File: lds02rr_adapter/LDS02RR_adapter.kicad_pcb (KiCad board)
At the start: 2 copper layers, 18.9 x 8.8 mm, 4 parts, among them J2 JST PH F 4P VERT, Q1 AS2302

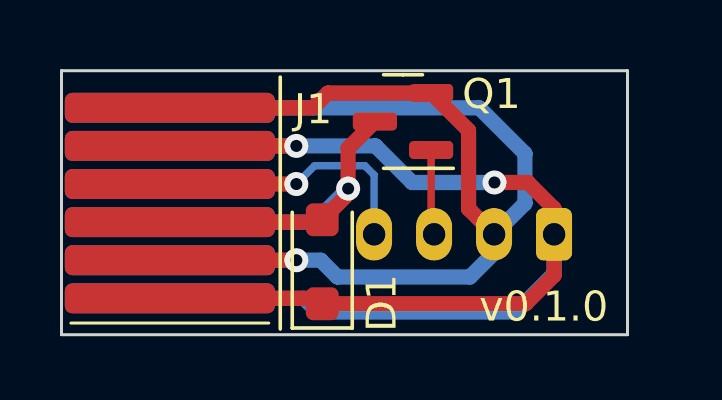
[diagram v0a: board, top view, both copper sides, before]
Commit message: Neato, LDS02RR v0.2.0
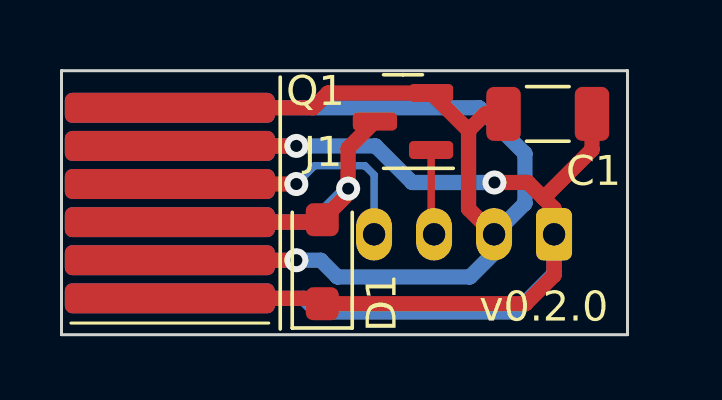
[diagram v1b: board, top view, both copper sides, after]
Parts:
- added C1: 100uF, Capacitor_SMD:C_1206_3216Metric, F.Cu at (156.2, 91.4)
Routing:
- net +5V: track 48.2 -> 51.7 mm
- net GND: track 46.3 -> 47.7 mm
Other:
- board text added: "v0.2.0"
- board text removed: "v0.1.0"
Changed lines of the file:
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@@
     (thickness 1.6)
   )
-  (paper "A4")
+  (paper "A5")
   (title_block
     (title "LDS02RR adapter")
-    (date "2023-12-21")
-    (rev "0.1.0")
+    (date "2024-01-30")
+    (rev "0.2.0")
     (company "Maker's Pet")
     (comment 1 "makerspet.com")
@@
       (drillshape 0)
       (scaleselection 1)
-      (outputdirectory "")
+      (outputdirectory "output/")
     )
   )
@@
     (property "ki_keywords" "LDS")
     (attr smd)
-    (fp_text reference "J1" (at 3.1242 4.7752 180) (layer "F.SilkS")
+    (fp_text reference "J1" (at 1.7018 5.1054 180) (layer "F.SilkS")
         (effects (font (size 1 1) (thickness 0.15)))
     )
@@
       (net 3 "GND") (pinfunction "GND") (pintype "passive") (thermal_bridge_angle 45))
   )
+  (footprint "Capacitor_SMD:C_1206_3216Metric" (layer "F.Cu")
+    (at 156.21 91.44 180)
+    (descr "Capacitor SMD 1206 (3216 Metric), square (rectangular) end terminal, IPC_7351 nominal, (Body size source: IPC-SM-782 page 76, https://www.pcb-3d.com/wordpress/wp-content/uploads/ipc-sm-782a_amendment_1_and_2.pdf), generated with kicad-footprint-generator")
+    (tags "capacitor")
+    (property "Sheetfile" "LDS02RR_adapter.kicad_sch")
+    (property "Sheetname" "")
+    (property "ki_description" "Unpolarized capacitor")
+    (property "ki_keywords" "cap capacitor")
+    (attr smd)
+    (fp_text reference "C1" (at -1.524 -1.905) (layer "F.SilkS")
+        (effects (font (size 1 1) (thickness 0.15)))
+    )
+    (fp_text value "100uF" (at 0 1.85) (layer "F.Fab") hide
+        (effects (font (size 1 1) (thickness 0.15)))
+    )
+    (fp_text user "${REFERENCE}" (at 0 0) (layer "F.Fab")
+        (effects (font (size 0.8 0.8) (thickness 0.12)))
+    )
+    (fp_line (start -0.711252 -0.91) (end 0.711252 -0.91)
+      (stroke (width 0.12) (type solid)) (layer "F.SilkS"))
+    (fp_line (start -0.711252 0.91) (end 0.711252 0.91)
+      (stroke (width 0.12) (type solid)) (layer "F.SilkS"))
+    (fp_line (start -2.3 -1.15) (end 2.3 -1.15)
+      (stroke (width 0.05) (type solid)) (layer "F.CrtYd"))
+    (fp_line (start -2.3 1.15) (end -2.3 -1.15)
+      (stroke (width 0.05) (type solid)) (layer "F.CrtYd"))
+    (fp_line (start 2.3 -1.15) (end 2.3 1.15)
+      (stroke (width 0.05) (type solid)) (layer "F.CrtYd"))
+    (fp_line (start 2.3 1.15) (end -2.3 1.15)
+      (stroke (width 0.05) (type solid)) (layer "F.CrtYd"))
+    (fp_line (start -1.6 -0.8) (end 1.6 -0.8)
+      (stroke (width 0.1) (type solid)) (layer "F.Fab"))
+    (fp_line (start -1.6 0.8) (end -1.6 -0.8)
+      (stroke (width 0.1) (type solid)) (layer "F.Fab"))
+    (fp_line (start 1.6 -0.8) (end 1.6 0.8)
+      (stroke (width 0.1) (type solid)) (layer "F.Fab"))
+    (fp_line (start 1.6 0.8) (end -1.6 0.8)
+      (stroke (width 0.1) (type solid)) (layer "F.Fab"))
+    (pad "1" smd roundrect (at -1.475 0 180) (size 1.15 1.8) (layers "F.Cu" "F.Paste" "F.Mask") (roundrect_rratio 0.2173913043)
+      (net 1 "+5V") (pintype "passive"))
+    (pad "2" smd roundrect (at 1.475 0 180) (size 1.15 1.8) (layers "F.Cu" "F.Paste" "F.Mask") (roundrect_rratio 0.2173913043)
+      (net 3 "GND") (pintype "passive"))
+    (model "${KICAD6_3DMODEL_DIR}/Capacitor_SMD.3dshapes/C_1206_3216Metric.wrl"
+      (offset (xyz 0 0 0))
+      (scale (xyz 1 1 1))
+      (rotate (xyz 0 0 0))
+    )
+  )
   (footprint "Diode_SMD:D_SOD-123F" (layer "F.Cu")
     (at 148.6916 96.3676 90)
@@
     (property "ki_keywords" "N-Channel MOSFET")
     (attr smd)
-    (fp_text reference "Q1" (at -2.9464 0.9144) (layer "F.SilkS")
+    (fp_text reference "Q1" (at 2.921 1.016) (layer "F.SilkS")
         (effects (font (size 1 1) (thickness 0.15)))
     )
@@
     (effects (font (size 1 1) (thickness 0.15)) (justify left bottom mirror))
   )
-  (gr_text "v0.1.0" (at 153.924 98.4504) (layer "F.SilkS")
+  (gr_text "v0.2.0" (at 153.924 98.4504) (layer "F.SilkS")
     (effects (font (size 1 1) (thickness 0.15)) (justify left bottom))
   )
+  (segment (start 157.685 92.632) (end 156.0703 94.2467) (width 0.508) (layer "F.Cu") (net 1))
   (segment (start 155.4704 97.7676) (end 156.4188 96.8192) (width 0.508) (layer "F.Cu") (net 1))
   (segment (start 143.6116 97.5868) (end 148.5108 97.5868) (width 0.508) (layer "F.Cu") (net 1))
   (segment (start 155.5496 93.726) (end 154.432 93.726) (width 0.508) (layer "F.Cu") (net 1))
+  (segment (start 156.0703 94.2467) (end 156.4188 94.5952) (width 0.508) (layer "F.Cu") (net 1))
   (segment (start 156.4188 94.5952) (end 156.4188 95.4532) (width 0.508) (layer "F.Cu") (net 1))
   (segment (start 148.7424 97.7676) (end 155.4704 97.7676) (width 0.508) (layer "F.Cu") (net 1))
-  (segment (start 155.5496 93.726) (end 156.4188 94.5952) (width 0.508) (layer "F.Cu") (net 1))
+  (segment (start 157.685 91.44) (end 157.685 92.632) (width 0.508) (layer "F.Cu") (net 1))
   (segment (start 148.5108 97.5868) (end 148.6916 97.7676) (width 0.508) (layer "F.Cu") (net 1))
+  (segment (start 155.5496 93.726) (end 156.0703 94.2467) (width 0.508) (layer "F.Cu") (net 1))
   (segment (start 156.4188 96.8192) (end 156.4188 95.4532) (width 0.508) (layer "F.Cu") (net 1))
   (segment (start 143.6116 92.5068) (end 147.828 92.5068) (width 0.508) (layer "F.Cu") (net 1))
@@
   (segment (start 143.6116 95.0468) (end 148.4376 95.0468) (width 0.508) (layer "B.Cu") (net 2))
   (segment (start 148.4376 95.0468) (end 149.5552 93.9292) (width 0.508) (layer "B.Cu") (net 2))
+  (segment (start 154.735 91.44) (end 154.1193 91.44) (width 0.508) (layer "F.Cu") (net 3))
   (segment (start 153.5684 91.9909) (end 153.5684 94.6028) (width 0.508) (layer "F.Cu") (net 3))
   (segment (start 153.5684 94.6028) (end 154.4188 95.4532) (width 0.508) (layer "F.Cu") (net 3))
   (segment (start 152.3215 90.744) (end 153.5684 91.9909) (width 0.508) (layer "F.Cu") (net 3))
   (segment (start 143.6116 91.2368) (end 148.3868 91.2368) (width 0.508) (layer "F.Cu") (net 3))
+  (segment (start 154.1193 91.44) (end 153.5684 91.9909) (width 0.508) (layer "F.Cu") (net 3))
   (segment (start 148.8796 90.744) (end 152.3215 90.744) (width 0.508) (layer "F.Cu") (net 3))
   (segment (start 143.6116 96.3168) (end 147.828 96.3168) (width 0.508) (layer "F.Cu") (net 3))

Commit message: 0603 bypass cap
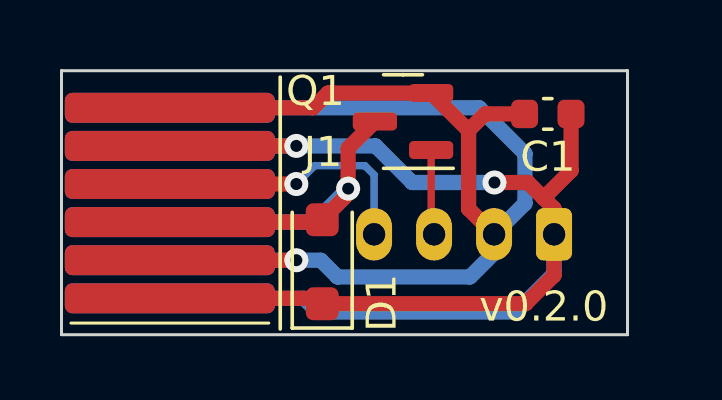
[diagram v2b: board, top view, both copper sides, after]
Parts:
- C1: value 100uF -> 22uF; footprint Capacitor_SMD:C_1206_3216Metric -> Capacitor_SMD:C_0603_1608Metric
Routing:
- net GND: track 47.7 -> 48.4 mm
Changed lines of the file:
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@@
   (title_block
     (title "LDS02RR adapter")
-    (date "2024-01-30")
-    (rev "0.2.0")
+    (date "2024-03-06")
+    (rev "0.2.1")
     (company "Maker's Pet")
     (comment 1 "makerspet.com")
@@
       (net 3 "GND") (pinfunction "GND") (pintype "passive") (thermal_bridge_angle 45))
   )
-  (footprint "Capacitor_SMD:C_1206_3216Metric" (layer "F.Cu")
+  (footprint "Capacitor_SMD:C_0603_1608Metric" (layer "F.Cu")
     (at 156.21 91.44 180)
-    (descr "Capacitor SMD 1206 (3216 Metric), square (rectangular) end terminal, IPC_7351 nominal, (Body size source: IPC-SM-782 page 76, https://www.pcb-3d.com/wordpress/wp-content/uploads/ipc-sm-782a_amendment_1_and_2.pdf), generated with kicad-footprint-generator")
+    (descr "Capacitor SMD 0603 (1608 Metric), square (rectangular) end terminal, IPC_7351 nominal, (Body size source: IPC-SM-782 page 76, https://www.pcb-3d.com/wordpress/wp-content/uploads/ipc-sm-782a_amendment_1_and_2.pdf), generated with kicad-footprint-generator")
     (tags "capacitor")
     (property "Sheetfile" "LDS02RR_adapter.kicad_sch")
@@
     (property "ki_keywords" "cap capacitor")
     (attr smd)
-    (fp_text reference "C1" (at -1.524 -1.905) (layer "F.SilkS")
-        (effects (font (size 1 1) (thickness 0.15)))
-    )
-    (fp_text value "100uF" (at 0 1.85) (layer "F.Fab") hide
-        (effects (font (size 1 1) (thickness 0.15)))
-    )
-    (fp_text user "${REFERENCE}" (at 0 0) (layer "F.Fab")
-        (effects (font (size 0.8 0.8) (thickness 0.12)))
-    )
-    (fp_line (start -0.711252 -0.91) (end 0.711252 -0.91)
-      (stroke (width 0.12) (type solid)) (layer "F.SilkS"))
-    (fp_line (start -0.711252 0.91) (end 0.711252 0.91)
-      (stroke (width 0.12) (type solid)) (layer "F.SilkS"))
-    (fp_line (start -2.3 -1.15) (end 2.3 -1.15)
-      (stroke (width 0.05) (type solid)) (layer "F.CrtYd"))
-    (fp_line (start -2.3 1.15) (end -2.3 -1.15)
-      (stroke (width 0.05) (type solid)) (layer "F.CrtYd"))
-    (fp_line (start 2.3 -1.15) (end 2.3 1.15)
-      (stroke (width 0.05) (type solid)) (layer "F.CrtYd"))
-    (fp_line (start 2.3 1.15) (end -2.3 1.15)
-      (stroke (width 0.05) (type solid)) (layer "F.CrtYd"))
-    (fp_line (start -1.6 -0.8) (end 1.6 -0.8)
-      (stroke (width 0.1) (type solid)) (layer "F.Fab"))
-    (fp_line (start -1.6 0.8) (end -1.6 -0.8)
-      (stroke (width 0.1) (type solid)) (layer "F.Fab"))
-    (fp_line (start 1.6 -0.8) (end 1.6 0.8)
-      (stroke (width 0.1) (type solid)) (layer "F.Fab"))
-    (fp_line (start 1.6 0.8) (end -1.6 0.8)
-      (stroke (width 0.1) (type solid)) (layer "F.Fab"))
-    (pad "1" smd roundrect (at -1.475 0 180) (size 1.15 1.8) (layers "F.Cu" "F.Paste" "F.Mask") (roundrect_rratio 0.2173913043)
+    (fp_text reference "C1" (at 0 -1.43 180) (layer "F.SilkS")
+        (effects (font (size 1 1) (thickness 0.15)))
+    )
+    (fp_text value "22uF" (at 0 1.43 180) (layer "F.Fab") hide
+        (effects (font (size 1 1) (thickness 0.15)))
+    )
+    (fp_text user "${REFERENCE}" (at 0 0 180) (layer "F.Fab")
+        (effects (font (size 0.4 0.4) (thickness 0.06)))
+    )
+    (fp_line (start -0.14058 -0.51) (end 0.14058 -0.51)
+      (stroke (width 0.12) (type solid)) (layer "F.SilkS"))
+    (fp_line (start -0.14058 0.51) (end 0.14058 0.51)
+      (stroke (width 0.12) (type solid)) (layer "F.SilkS"))
+    (fp_line (start -1.48 -0.73) (end 1.48 -0.73)
+      (stroke (width 0.05) (type solid)) (layer "F.CrtYd"))
+    (fp_line (start -1.48 0.73) (end -1.48 -0.73)
+      (stroke (width 0.05) (type solid)) (layer "F.CrtYd"))
+    (fp_line (start 1.48 -0.73) (end 1.48 0.73)
+      (stroke (width 0.05) (type solid)) (layer "F.CrtYd"))
+    (fp_line (start 1.48 0.73) (end -1.48 0.73)
+      (stroke (width 0.05) (type solid)) (layer "F.CrtYd"))
+    (fp_line (start -0.8 -0.4) (end 0.8 -0.4)
+      (stroke (width 0.1) (type solid)) (layer "F.Fab"))
+    (fp_line (start -0.8 0.4) (end -0.8 -0.4)
+      (stroke (width 0.1) (type solid)) (layer "F.Fab"))
+    (fp_line (start 0.8 -0.4) (end 0.8 0.4)
+      (stroke (width 0.1) (type solid)) (layer "F.Fab"))
+    (fp_line (start 0.8 0.4) (end -0.8 0.4)
+      (stroke (width 0.1) (type solid)) (layer "F.Fab"))
+    (pad "1" smd roundrect (at -0.775 0 180) (size 0.9 0.95) (layers "F.Cu" "F.Paste" "F.Mask") (roundrect_rratio 0.25)
       (net 1 "+5V") (pintype "passive"))
-    (pad "2" smd roundrect (at 1.475 0 180) (size 1.15 1.8) (layers "F.Cu" "F.Paste" "F.Mask") (roundrect_rratio 0.2173913043)
+    (pad "2" smd roundrect (at 0.775 0 180) (size 0.9 0.95) (layers "F.Cu" "F.Paste" "F.Mask") (roundrect_rratio 0.25)
       (net 3 "GND") (pintype "passive"))
-    (model "${KICAD6_3DMODEL_DIR}/Capacitor_SMD.3dshapes/C_1206_3216Metric.wrl"
+    (model "${KICAD6_3DMODEL_DIR}/Capacitor_SMD.3dshapes/C_0603_1608Metric.wrl"
       (offset (xyz 0 0 0))
       (scale (xyz 1 1 1))
@@
     (effects (font (size 1 1) (thickness 0.15)) (justify left bottom))
   )
-  (segment (start 157.685 92.632) (end 156.0703 94.2467) (width 0.508) (layer "F.Cu") (net 1))
+  (segment (start 156.985 93.332) (end 156.0703 94.2467) (width 0.508) (layer "F.Cu") (net 1))
   (segment (start 155.4704 97.7676) (end 156.4188 96.8192) (width 0.508) (layer "F.Cu") (net 1))
   (segment (start 143.6116 97.5868) (end 148.5108 97.5868) (width 0.508) (layer "F.Cu") (net 1))
   (segment (start 155.5496 93.726) (end 154.432 93.726) (width 0.508) (layer "F.Cu") (net 1))
+  (segment (start 156.985 91.44) (end 156.985 93.332) (width 0.508) (layer "F.Cu") (net 1))
   (segment (start 156.0703 94.2467) (end 156.4188 94.5952) (width 0.508) (layer "F.Cu") (net 1))
   (segment (start 156.4188 94.5952) (end 156.4188 95.4532) (width 0.508) (layer "F.Cu") (net 1))
   (segment (start 148.7424 97.7676) (end 155.4704 97.7676) (width 0.508) (layer "F.Cu") (net 1))
-  (segment (start 157.685 91.44) (end 157.685 92.632) (width 0.508) (layer "F.Cu") (net 1))
   (segment (start 148.5108 97.5868) (end 148.6916 97.7676) (width 0.508) (layer "F.Cu") (net 1))
   (segment (start 155.5496 93.726) (end 156.0703 94.2467) (width 0.508) (layer "F.Cu") (net 1))
@@
   (segment (start 143.6116 95.0468) (end 148.4376 95.0468) (width 0.508) (layer "B.Cu") (net 2))
   (segment (start 148.4376 95.0468) (end 149.5552 93.9292) (width 0.508) (layer "B.Cu") (net 2))
-  (segment (start 154.735 91.44) (end 154.1193 91.44) (width 0.508) (layer "F.Cu") (net 3))
   (segment (start 153.5684 91.9909) (end 153.5684 94.6028) (width 0.508) (layer "F.Cu") (net 3))
   (segment (start 153.5684 94.6028) (end 154.4188 95.4532) (width 0.508) (layer "F.Cu") (net 3))
+  (segment (start 154.1193 91.44) (end 155.435 91.44) (width 0.508) (layer "F.Cu") (net 3))
   (segment (start 152.3215 90.744) (end 153.5684 91.9909) (width 0.508) (layer "F.Cu") (net 3))
   (segment (start 143.6116 91.2368) (end 148.3868 91.2368) (width 0.508) (layer "F.Cu") (net 3))
